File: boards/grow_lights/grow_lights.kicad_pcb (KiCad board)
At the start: 2 copper layers, 99.3 x 100.1 mm, 11 parts, among them J11 LED Connector

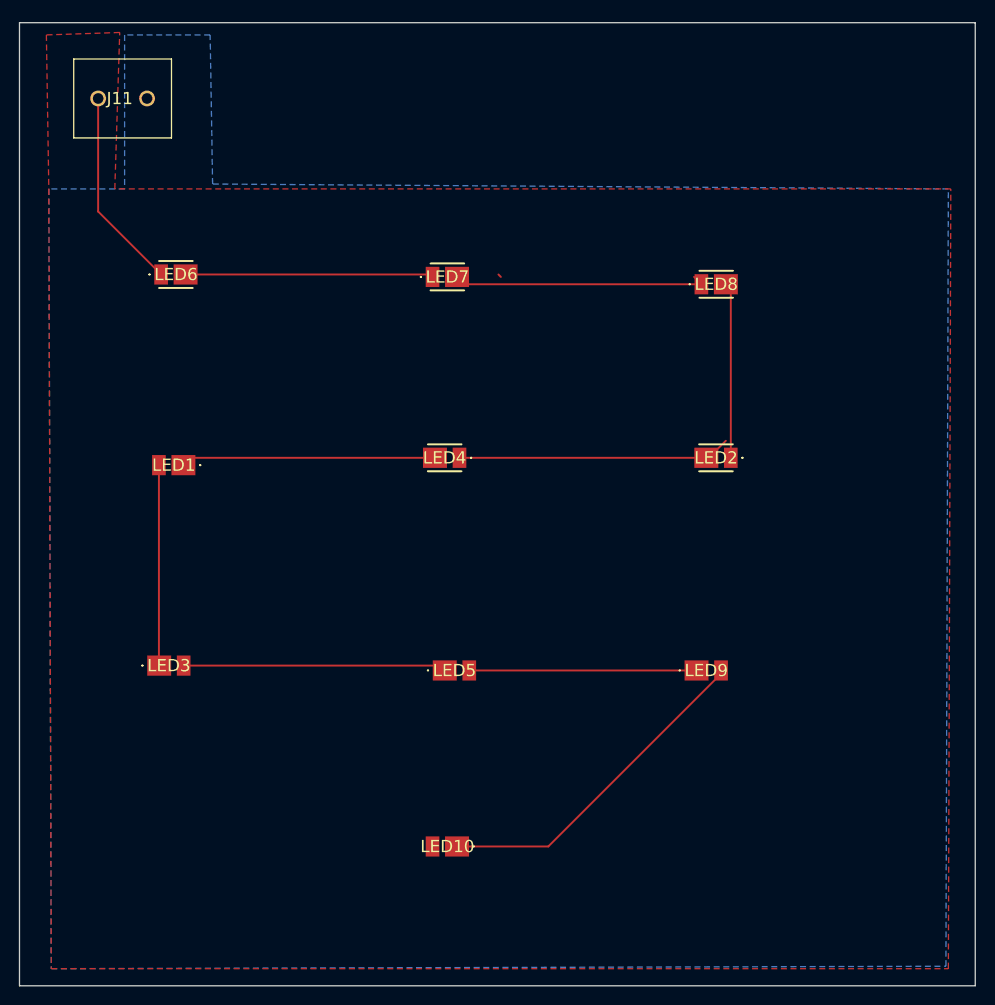
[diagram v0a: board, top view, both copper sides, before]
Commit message: updated grow lights board with wider traces & removed power plane
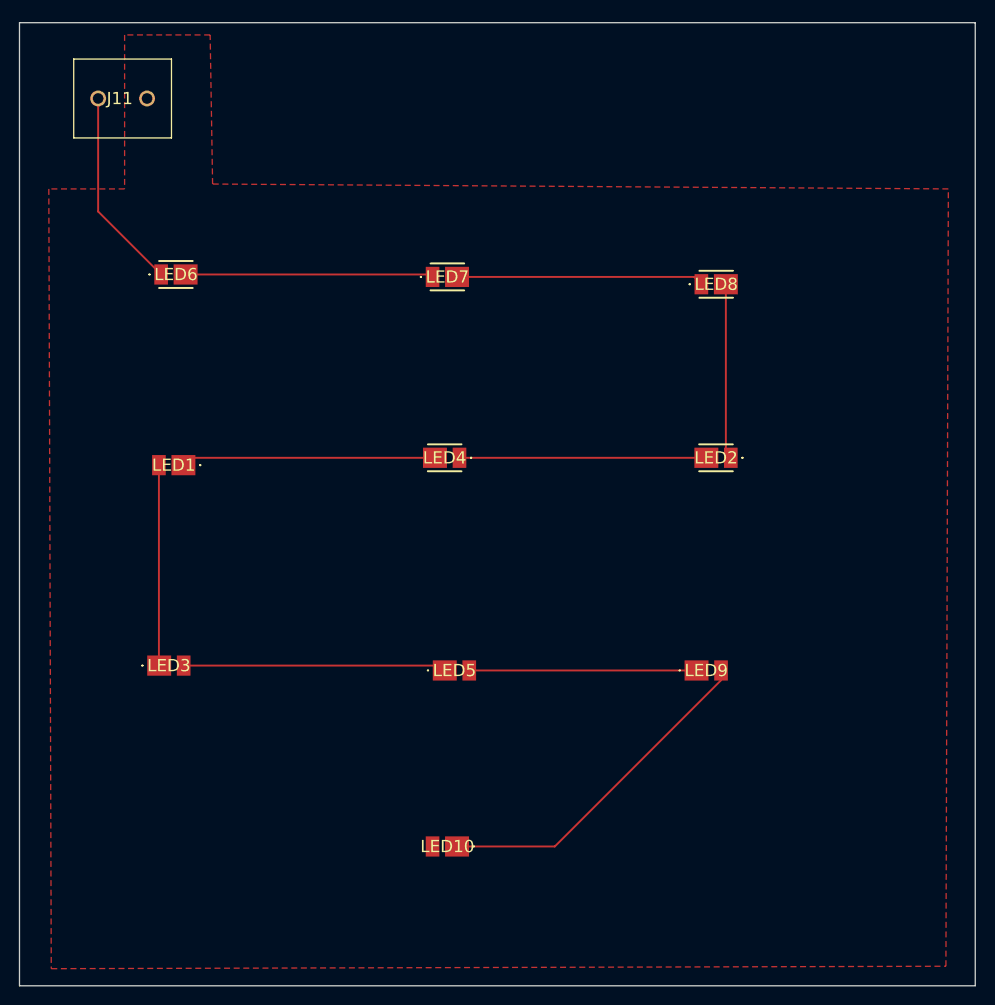
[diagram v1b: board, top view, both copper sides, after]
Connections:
- LED10 pad 2: GND -> LED-
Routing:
- net Net-(LED2-K): track 28.2 -> 26.0 mm
- net Net-(LED2-A): track 18.2 -> 19.0 mm
- added copper zone on F.Cu, net LED-
- removed copper zone on B.Cu, net LED-
- removed copper zone on F.Cu, net LEDS
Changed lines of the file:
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@@
 	(net 10 "Net-(LED7-K)")
 	(net 11 "Net-(LED10-A)")
-	(net 12 "GND")
 	(footprint "SamacSys_Parts:2828372"
 		(layer "F.Cu")
@@
 			(size 1.42 2.1)
 			(layers "F.Cu" "F.Mask" "F.Paste")
-			(net 12 "GND")
+			(net 1 "LED-")
 			(pinfunction "K")
 			(pintype "passive")
@@
 	)
 	(segment
-		(start 145.537 96.266)
-		(end 120.158 96.266)
+		(start 120.158 96.266)
+		(end 119.396 97.028)
 		(width 0.2)
 		(layer "F.Cu")
@@
 	)
 	(segment
-		(start 120.158 96.266)
-		(end 119.396 97.028)
+		(start 145.537 96.266)
+		(end 120.158 96.266)
 		(width 0.2)
 		(layer "F.Cu")
@@
 	)
 	(segment
-		(start 116.851 97.028)
-		(end 116.851 117.829)
+		(start 116.851 117.829)
+		(end 116.878 117.856)
 		(width 0.2)
 		(layer "F.Cu")
@@
 	)
 	(segment
-		(start 116.851 117.829)
-		(end 116.878 117.856)
+		(start 116.851 97.028)
+		(end 116.851 117.829)
 		(width 0.2)
 		(layer "F.Cu")
@@
 	)
 	(segment
-		(start 175.762 94.494)
-		(end 174.244 96.012)
+		(start 173.731 96.266)
+		(end 148.082 96.266)
 		(width 0.2)
 		(layer "F.Cu")
@@
 	)
 	(segment
-		(start 173.731 96.266)
-		(end 148.082 96.266)
+		(start 175.762 95.752)
+		(end 176.276 96.266)
 		(width 0.2)
 		(layer "F.Cu")
-		(net 5)
+		(net 6)
 	)
 	(segment
 		(start 175.762 78.232)
-		(end 176.276 78.746)
+		(end 175.762 95.752)
 		(width 0.2)
 		(layer "F.Cu")
@@
 	)
 	(segment
-		(start 176.276 78.746)
-		(end 176.276 96.266)
+		(start 175.762 78.232)
+		(end 176.276 78.746)
 		(width 0.2)
 		(layer "F.Cu")
@@
 	)
 	(segment
-		(start 152.13 77.216)
-		(end 152.384 77.47)
-		(width 0.2)
-		(layer "F.Cu")
-		(net 9)
-	)
-	(segment
 		(start 145.029 77.216)
 		(end 145.283 77.47)
@@
 	)
 	(segment
-		(start 172.455 77.47)
-		(end 173.217 78.232)
+		(start 147.828 77.47)
+		(end 148.59 78.232)
 		(width 0.2)
 		(layer "F.Cu")
@@
 	)
 	(segment
-		(start 148.59 78.232)
+		(start 172.455 77.47)
 		(end 173.217 78.232)
 		(width 0.2)
@@
 	(segment
 		(start 147.828 77.47)
-		(end 148.59 78.232)
+		(end 172.455 77.47)
 		(width 0.2)
 		(layer "F.Cu")
@@
 	)
 	(segment
-		(start 175.26 118.704)
-		(end 157.312 136.652)
+		(start 175.26 118.364)
+		(end 175.26 119.38)
 		(width 0.2)
 		(layer "F.Cu")
@@
 	)
 	(segment
-		(start 175.26 118.364)
-		(end 175.26 118.704)
+		(start 157.988 136.652)
+		(end 147.828 136.652)
 		(width 0.2)
 		(layer "F.Cu")
@@
 	)
 	(segment
-		(start 157.312 136.652)
-		(end 147.828 136.652)
+		(start 175.26 119.38)
+		(end 157.988 136.652)
 		(width 0.2)
 		(layer "F.Cu")
@@
 	)
 	(zone
-		(net 2)
-		(net_name "LEDS")
-		(layer "F.Cu")
-		(hatch edge 0.5)
-		(connect_pads
-			(clearance 0.5)
-		)
-		(min_thickness 0.25)
-		(filled_areas_thickness no)
-		(fill yes
-			(thermal_gap 0.5)
-			(thermal_bridge_width 0.5)
-		)
-		(polygon
-			(pts
-				(xy 105.41 68.326) (xy 105.664 149.352) (xy 198.882 149.352) (xy 199.136 68.326) (xy 112.268 68.326)
-				(xy 112.776 52.07) (xy 105.156 52.324)
-			)
-		)
-	)
-	(zone
 		(net 1)
 		(net_name "LED-")
-		(layer "B.Cu")
+		(layer "F.Cu")
 		(hatch edge 0.5)
 		(priority 1)

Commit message: made LED- the back copper
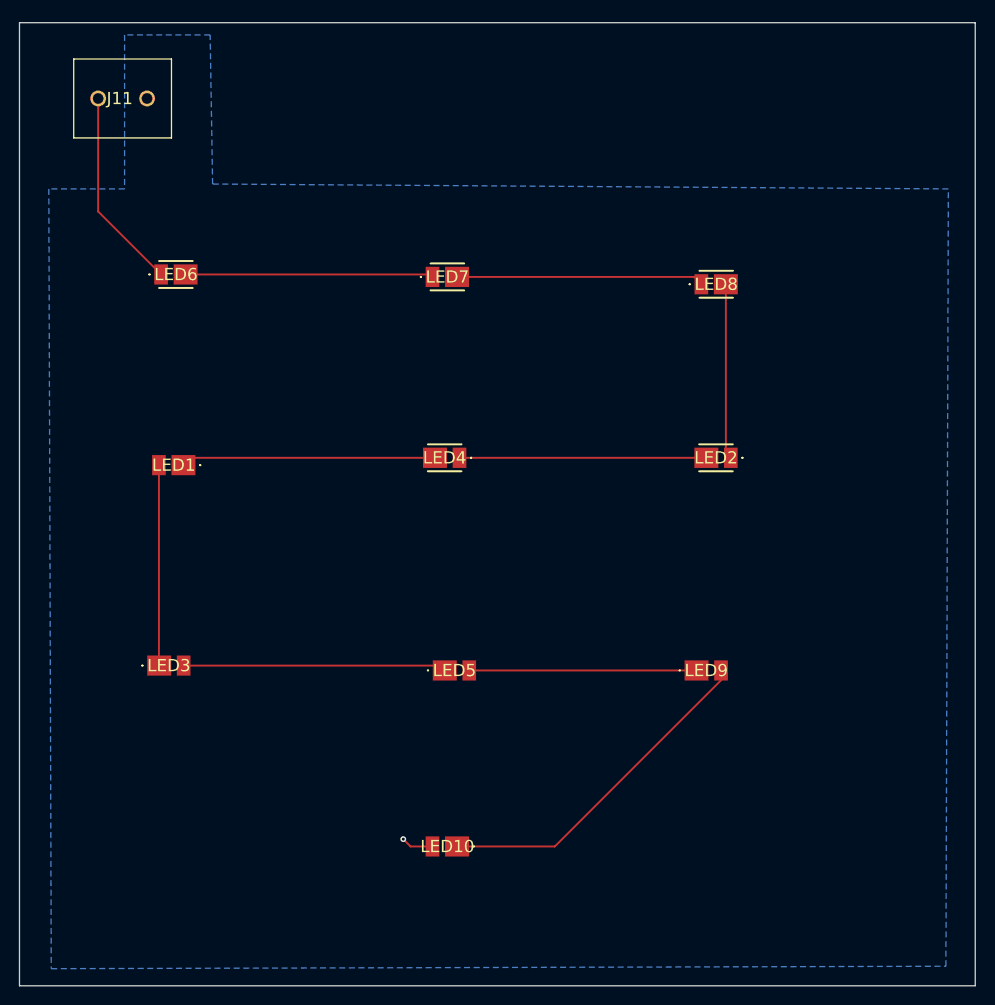
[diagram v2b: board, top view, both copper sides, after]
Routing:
- net LED-: track 0.00 -> 3.36 mm, vias 0 -> 1
- added copper zone on B.Cu, net LED-
- removed copper zone on F.Cu, net LED-
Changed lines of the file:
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@@
+	)
+	(segment
+		(start 142.24 135.89)
+		(end 143.002 136.652)
+		(width 0.2)
+		(layer "F.Cu")
+		(net 1)
+	)
+	(segment
+		(start 143.002 136.652)
+		(end 145.283 136.652)
+		(width 0.2)
+		(layer "F.Cu")
+		(net 1)
+	)
+	(via
+		(at 142.24 135.89)
+		(size 0.6)
+		(drill 0.3)
+		(layers "F.Cu" "B.Cu")
+		(free yes)
+		(net 1)
 	)
 	(segment
@@
 		(net 1)
 		(net_name "LED-")
-		(layer "F.Cu")
+		(layer "B.Cu")
 		(hatch edge 0.5)
 		(priority 1)

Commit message: finished generating files and put them in files folder for each PCB, also have zipped them
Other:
- board text added: "Team 73 Circle of Life LED V1"
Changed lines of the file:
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@@
 			(usegerberattributes yes)
 			(usegerberadvancedattributes yes)
-			(creategerberjobfile yes)
+			(creategerberjobfile no)
 			(dashed_line_dash_ratio 12.000000)
 			(dashed_line_gap_ratio 3.000000)
@@
 			(outputformat 1)
 			(mirror no)
-			(drillshape 1)
+			(drillshape 0)
 			(scaleselection 1)
 			(outputdirectory "")
@@
 		(layer "Edge.Cuts")
 	)
+	(gr_text "Team 73 \nCircle of Life LED V1"
+		(at 135.89 109.22 0)
+		(layer "F.SilkS")
+		(effects
+			(font
+				(size 2 2)
+				(thickness 0.2)
+				(bold yes)
+			)
+			(justify left bottom)
+		)
+	)
 	(segment
 		(start 142.24 135.89)
 		(end 143.002 136.652)
-		(width 0.2)
+		(width 1.3)
 		(layer "F.Cu")
 		(net 1)
@@
 		(start 143.002 136.652)
 		(end 145.283 136.652)
-		(width 0.2)
+		(width 1.3)
 		(layer "F.Cu")
 		(net 1)
@@
 	(via
 		(at 142.24 135.89)
-		(size 0.6)
-		(drill 0.3)
+		(size 1.3)
+		(drill 0.8)
 		(layers "F.Cu" "B.Cu")
 		(free yes)
@@
 		(start 110.536 70.674)
 		(end 117.078 77.216)
-		(width 0.2)
+		(width 1.3)
 		(layer "F.Cu")
 		(net 2)
@@
 		(start 110.536 58.928)
 		(end 110.536 70.674)
-		(width 0.2)
+		(width 1.3)
 		(layer "F.Cu")
 		(net 2)
@@
 		(start 145.537 96.266)
 		(end 120.158 96.266)
-		(width 0.2)
+		(width 1.3)
 		(layer "F.Cu")
 		(net 3)
@@
 		(start 116.851 97.028)
 		(end 116.851 117.829)
-		(width 0.2)
+		(width 1.3)
 		(layer "F.Cu")
 		(net 4)
@@
 		(start 173.731 96.266)
 		(end 148.082 96.266)
-		(width 0.2)
+		(width 1.3)
 		(layer "F.Cu")
 		(net 5)
@@
 		(start 175.762 78.232)
 		(end 175.762 95.752)
-		(width 0.2)
+		(width 1.3)
 		(layer "F.Cu")
 		(net 6)
@@
 		(start 119.423 117.856)
 		(end 146.045 117.856)
-		(width 0.2)
+		(width 1.3)
 		(layer "F.Cu")
 		(net 7)
@@
 		(start 149.098 118.364)
 		(end 172.715 118.364)
-		(width 0.2)
+		(width 1.3)
 		(layer "F.Cu")
 		(net 8)
@@
 		(start 119.623 77.216)
 		(end 145.029 77.216)
-		(width 0.2)
+		(width 1.3)
 		(layer "F.Cu")
 		(net 9)
@@
 		(start 147.828 77.47)
 		(end 172.455 77.47)
-		(width 0.2)
+		(width 1.3)
 		(layer "F.Cu")
 		(net 10)
@@
 		(start 157.988 136.652)
 		(end 147.828 136.652)
-		(width 0.2)
+		(width 1.3)
 		(layer "F.Cu")
 		(net 11)
@@
 		(start 175.26 119.38)
 		(end 157.988 136.652)
-		(width 0.2)
+		(width 1.3)
 		(layer "F.Cu")
 		(net 11)

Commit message: grow lights PCB
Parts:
- added H1: MountingHole, MountingHole:MountingHole_3.2mm_M3, F.Cu at (196.8, 55.9)
- added H2: MountingHole, MountingHole:MountingHole_3.2mm_M3, F.Cu at (196.8, 146.1)
- added H3: MountingHole, MountingHole:MountingHole_3.2mm_M3, F.Cu at (108.0, 146.1)
- added H4: MountingHole, MountingHole:MountingHole_3.2mm_M3, F.Cu at (108.0, 55.9)
- moved J11 27.9 mm to (138.4, 59.7)
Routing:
- net LEDS: track 21.0 -> 33.1 mm

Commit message: code and grow lights pcb updates
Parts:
- LED2, LED4, LED6, LED7, LED8: footprint SamacSys_Parts:ASMWL300AFH0E -> SamacSys_Parts:ASMWLL00NKM0E
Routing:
- net Net-(LED7-K): track 26.8 -> 27.9 mm
- net Net-(LED2-A): track 19.0 -> 19.7 mm
- net Net-(LED1-A): track 26.5 -> 25.9 mm

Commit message: Updated grow lights board
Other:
- board text added: "Team 73 Circle of Life LED V4"
- board text removed: "Team 73 Circle of Life LED V1"
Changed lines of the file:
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@@
 			(plot_on_all_layers_selection 0x00000000_00000000_00000000_00000000)
 			(disableapertmacros no)
-			(usegerberextensions yes)
+			(usegerberextensions no)
 			(usegerberattributes yes)
 			(usegerberadvancedattributes yes)
@@
 			(drillshape 0)
 			(scaleselection 1)
-			(outputdirectory "")
+			(outputdirectory "files_v3/")
 		)
 	)
@@
 		(layer "Edge.Cuts")
 	)
-	(gr_text "Team 73 \nCircle of Life LED V1"
+	(gr_text "Team 73 \nCircle of Life LED V4"
 		(at 135.89 109.22 0)
 		(layer "F.SilkS")
